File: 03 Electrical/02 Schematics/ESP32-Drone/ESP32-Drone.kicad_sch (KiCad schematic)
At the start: 0 parts

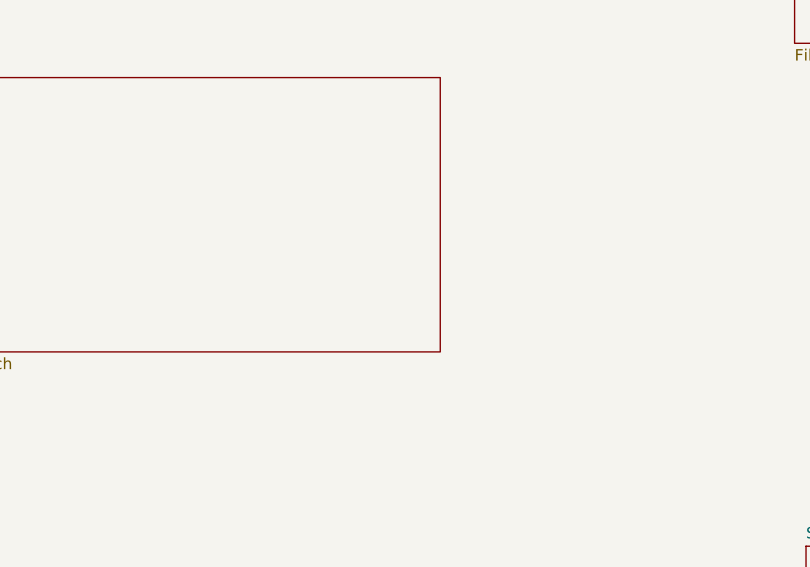
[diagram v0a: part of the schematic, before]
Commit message: started placing the esp32 circuitry
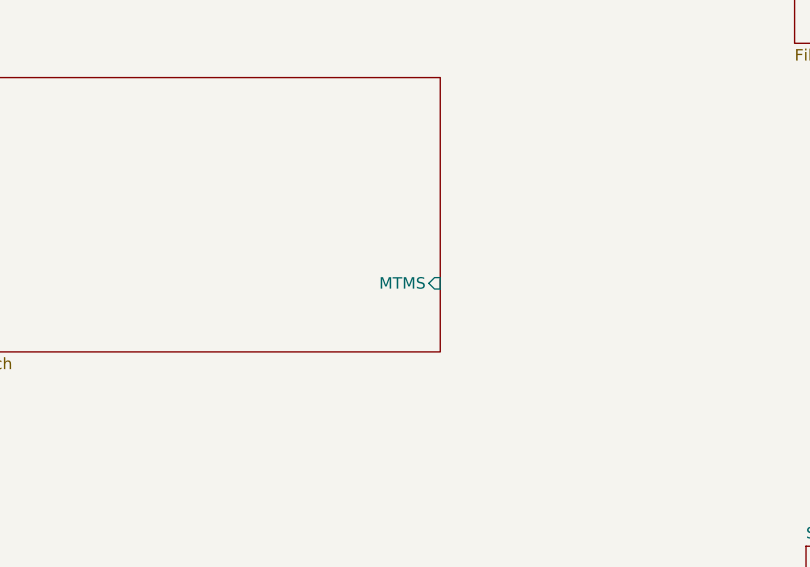
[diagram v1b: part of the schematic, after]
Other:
- sheet ESP32 ports: added MTMS; removed none
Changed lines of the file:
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@@
+			)
+		)
+		(pin "MTMS" input
+			(at 228.6 105.41 0)
+			(effects
+				(font
+					(size 1.27 1.27)
+				)
+				(justify right)
 			)
 		)
